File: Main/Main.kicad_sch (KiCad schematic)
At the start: 58 parts, among them J1 Conn_02x16_Odd_Even, J2 TYPE-C 6P, Q3 S9013 J3(RANGE:200-350), SW2 SS-12D11G3R, U1 BQ24074RGT, U2 DRV8833PW, U3 HUSB237-AA001-DN06R, U4 RT9742GGJ5, U5 RT9742GGJ5, U6 INA219AxDCN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

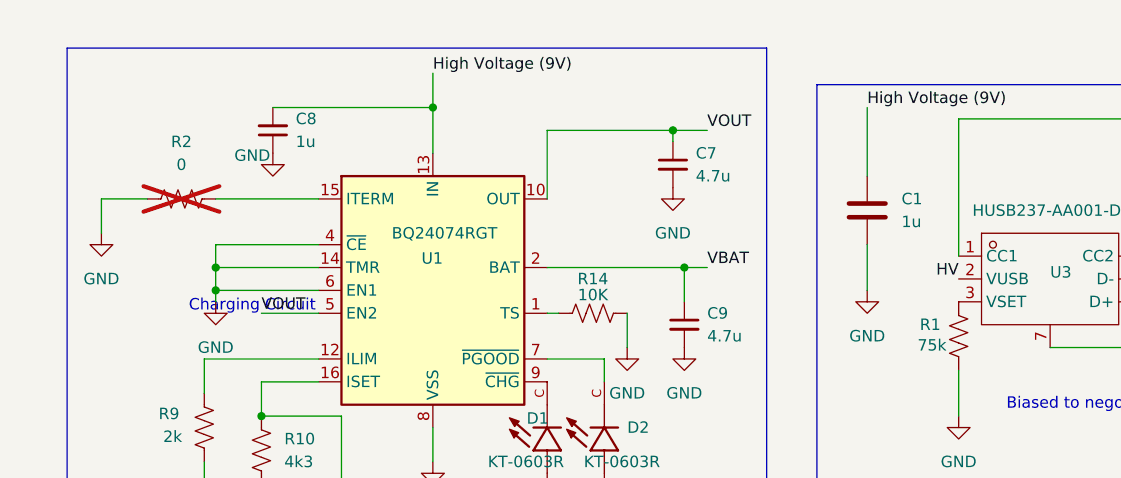
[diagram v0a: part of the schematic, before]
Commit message: Some few fixes on pin assignments
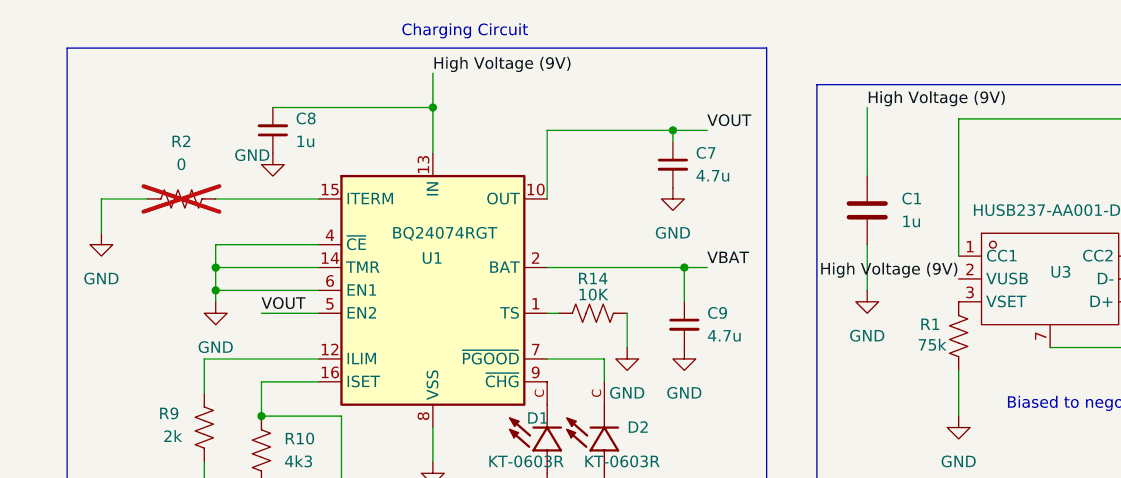
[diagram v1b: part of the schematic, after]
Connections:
- net HV is gone; now on net High Voltage (9V): U3.2 (VUSB)
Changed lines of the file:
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@@
 	(text "Charging Circuit\n"
 		(exclude_from_sim no)
-		(at 66.294 44.958 0)
+		(at 89.916 14.478 0)
 		(effects
 			(font
@@
 	(wire
 		(pts
+			(xy 140.97 218.44) (xy 140.97 220.98)
+		)
+		(stroke
+			(width 0)
+			(type default)
+		)
+	)
+	(wire
+		(pts
+			(xy 163.83 93.98) (xy 162.56 93.98)
+		)
+		(stroke
+			(width 0)
+			(type default)
+		)
+	)
+	(wire
+		(pts
+			(xy 364.49 58.42) (xy 389.89 58.42)
+		)
+		(stroke
+			(width 0)
+			(type default)
+		)
+	)
+	(wire
+		(pts
+			(xy 196.85 172.72) (xy 200.66 172.72)
+		)
+		(stroke
+			(width 0)
+			(type default)
+		)
+	)
+	(wire
+		(pts
+			(xy 217.17 232.41) (xy 220.98 232.41)
+		)
+		(stroke
+			(width 0)
+			(type default)
+		)
+	)
+	(wire
+		(pts
+			(xy 162.56 99.06) (xy 162.56 93.98)
+		)
+		(stroke
+			(width 0)
+			(type default)
+		)
+	)
+	(wire
+		(pts
 			(xy 190.5 41.91) (xy 194.31 41.91)
-		)
-		(stroke
-			(width 0)
-			(type default)
-		)
-	)
-	(wire
-		(pts
-			(xy 140.97 218.44) (xy 140.97 220.98)
-		)
-		(stroke
-			(width 0)
-			(type default)
-		)
-	)
-	(wire
-		(pts
-			(xy 163.83 93.98) (xy 162.56 93.98)
-		)
-		(stroke
-			(width 0)
-			(type default)
-		)
-	)
-	(wire
-		(pts
-			(xy 364.49 58.42) (xy 389.89 58.42)
-		)
-		(stroke
-			(width 0)
-			(type default)
-		)
-	)
-	(wire
-		(pts
-			(xy 196.85 172.72) (xy 200.66 172.72)
-		)
-		(stroke
-			(width 0)
-			(type default)
-		)
-	)
-	(wire
-		(pts
-			(xy 217.17 232.41) (xy 220.98 232.41)
-		)
-		(stroke
-			(width 0)
-			(type default)
-		)
-	)
-	(wire
-		(pts
-			(xy 162.56 99.06) (xy 162.56 93.98)
 		)
 		(stroke
@@
 		)
 	)
-	(label "HV"
+	(label "High Voltage (9V)"
 		(at 144.78 41.91 180)
 		(effects

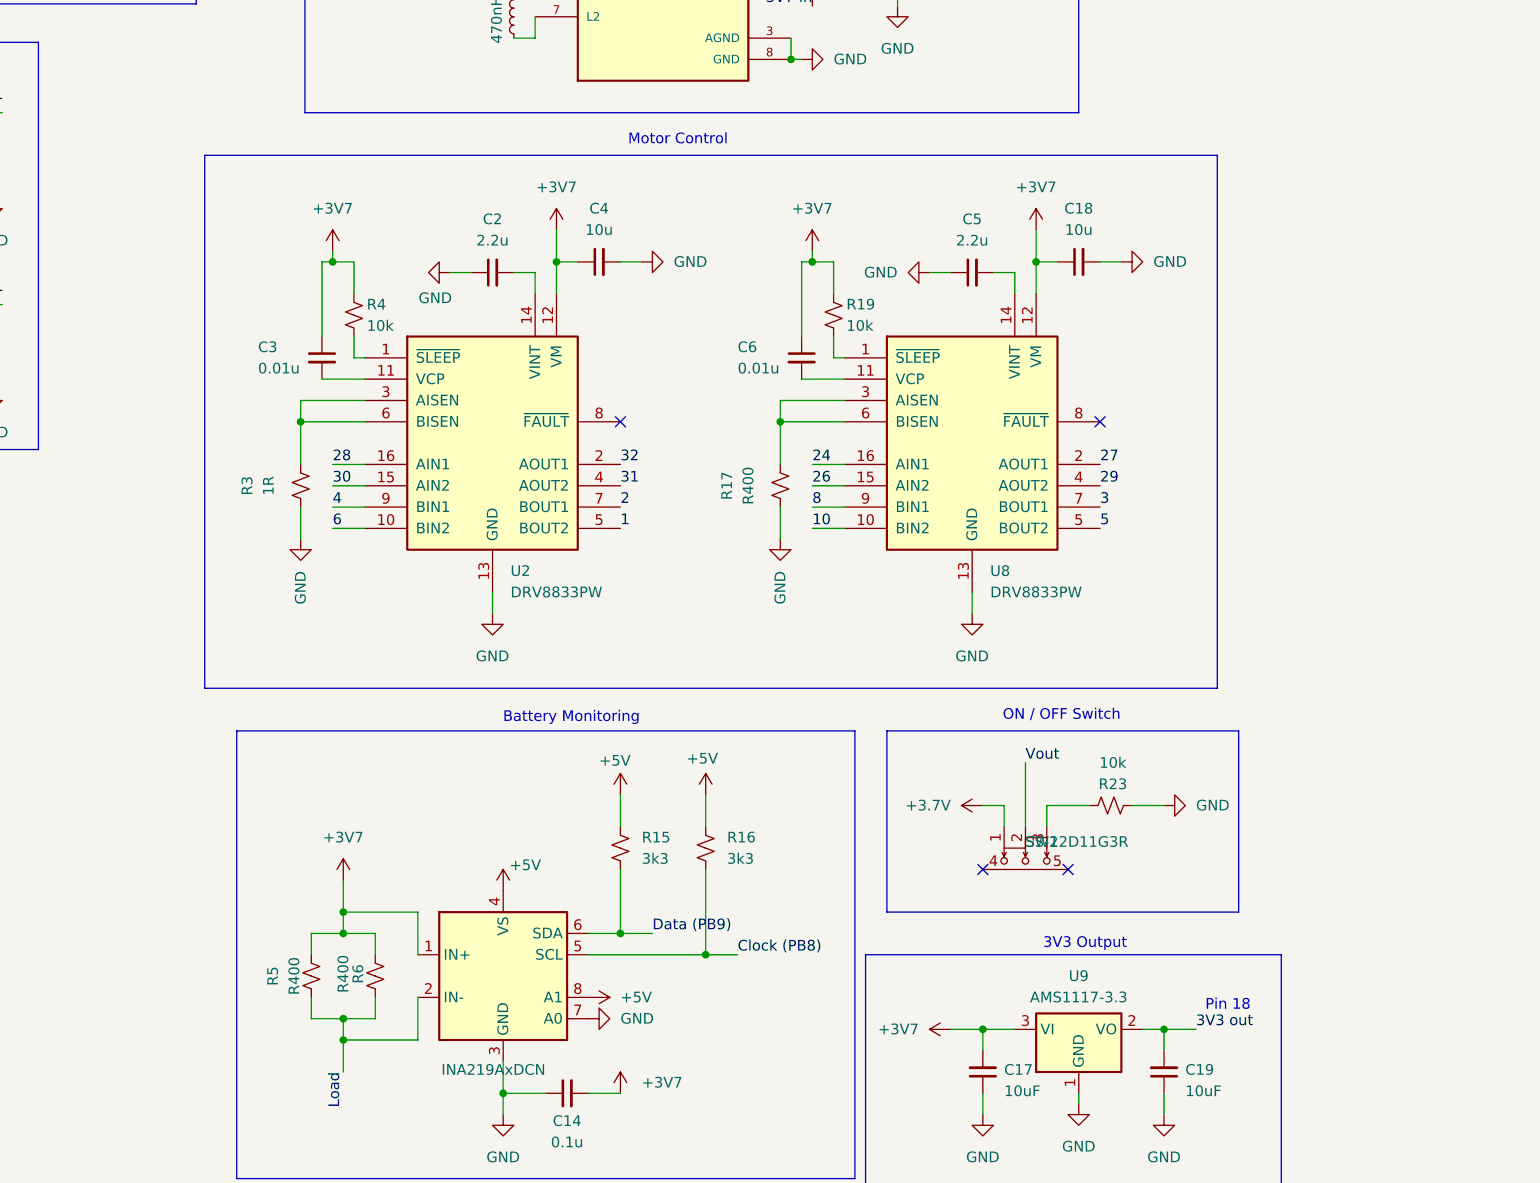
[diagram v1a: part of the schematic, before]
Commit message: Changed pins
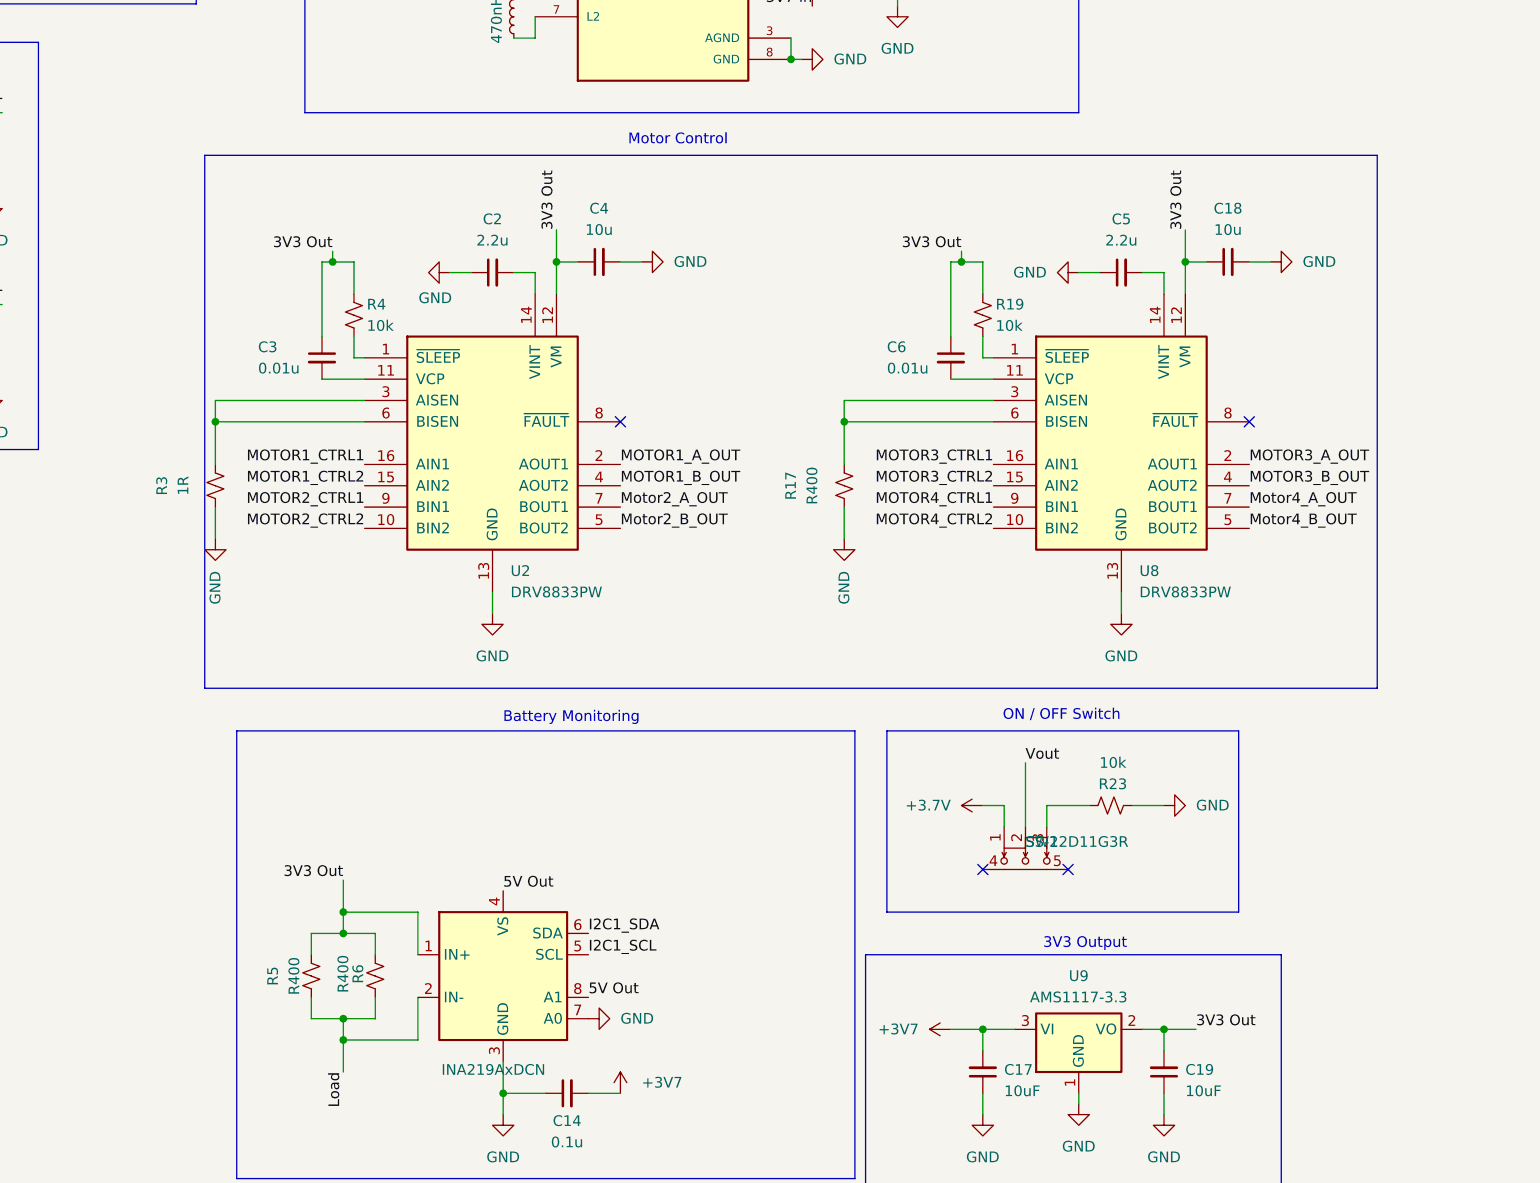
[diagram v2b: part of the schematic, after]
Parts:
- removed R15, R16: 3k3, Resistor_SMD:R_0603_1608Metric_Pad0.98x0.95mm_HandSolder, symbol Device:R_Small_US
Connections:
- net +5V is gone; now on net 5V Out: U6.4 (VS), U6.8 (A1)
- net 1 is gone; now on net Motor2_B_OUT: U2.5 (BOUT2)
- net 10 is gone; now on net MOTOR4_CTRL2: U8.10 (BIN2)
- net 2 is gone; now on net Motor2_A_OUT: U2.7 (BOUT1)
- net 24 is gone; now on net MOTOR3_CTRL1: U8.16 (AIN1)
- net 26 is gone; now on net MOTOR3_CTRL2: U8.15 (AIN2)
- net 27 is gone; now on net MOTOR3_A_OUT: U8.2 (AOUT1)
- net 28 is gone; now on net MOTOR1_CTRL1: U2.16 (AIN1)
- net 29 is gone; now on net MOTOR3_B_OUT: U8.4 (AOUT2)
- net 3 is gone; now on net Motor4_A_OUT: U8.7 (BOUT1)
- net 30 is gone; now on net MOTOR1_CTRL2: U2.15 (AIN2)
- net 31 is gone; now on net MOTOR1_B_OUT: U2.4 (AOUT2)
- net 32 is gone; now on net MOTOR1_A_OUT: U2.2 (AOUT1)
- net 3V3 out is gone; now on net 3V3 Out: C19.2, U9.2 (VO)
- net 4 is gone; now on net MOTOR2_CTRL1: U2.9 (BIN1)
- net 5 is gone; now on net Motor4_B_OUT: U8.5 (BOUT2)
- net 6 is gone; now on net MOTOR2_CTRL2: U2.10 (BIN2)
- net 8 is gone; now on net MOTOR4_CTRL1: U8.9 (BIN1)
- net Clock (PB8) is gone; now on net I2C1_SCL: U6.5 (SCL)
- net Data (PB9) is gone; now on net I2C1_SDA: U6.6 (SDA)
- net +3V7: no longer C18.1, C3.1, C4.1, C6.1, R19.1, R4.1, R5.2, R6.2, U2.12 (VM), U6.1 (IN+), U8.12 (VM)
- net 3V3 Out: now also C18.1, C3.1, C4.1, C6.1, R19.1, R4.1, R5.2, R6.2, U2.12 (VM), U6.1 (IN+), U8.12 (VM)
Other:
- note removed: "Pin 18"
- moved on the sheet: C18, C5, C6, R17, R19, R3, U8

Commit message: Changed Some Pin Names
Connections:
- net VBAT is gone; now on net Battery: C9.1, U1.2 (BAT), U1.3 (BAT)
- net Vout is gone; now on net switch: SW2.2
- net +3V7: no longer C17.2, U9.3 (VI)
- net 3V7 in renamed switch
- net switch: now also C17.2, U9.3 (VI)
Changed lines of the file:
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@@
 	(wire
 		(pts
+			(xy 196.85 110.49) (xy 196.85 113.03)
+		)
+		(stroke
+			(width 0)
+			(type default)
+		)
+	)
+	(wire
+		(pts
 			(xy 99.06 148.59) (xy 99.06 156.21)
 		)
@@
 		)
 	)
+	(label "switch"
+		(at 162.56 90.17 0)
+		(effects
+			(font
+				(size 1.27 1.27)
+			)
+			(justify left bottom)
+		)
+	)
 	(label "MOTOR2_CTRL2"
 		(at 351.79 35.56 180)
@@
 		)
 	)
-	(label "3V7 in"
-		(at 196.85 110.49 180)
+	(label "MOTOR3_B_OUT"
+		(at 248.92 167.64 0)
 		(effects
 			(font
 				(size 1.27 1.27)
 			)
-			(justify right bottom)
+			(justify left bottom)
 		)
 	)
-	(label "MOTOR3_B_OUT"
-		(at 248.92 167.64 0)
+	(label "switch"
+		(at 196.85 113.03 0)
 		(effects
 			(font
@@
 		)
 	)
-	(label "Vout"
+	(label "switch"
 		(at 222.25 200.66 0)
 		(effects
@@
 		)
 	)
-	(label "3V7 in"
-		(at 162.56 90.17 180)
-		(effects
-			(font
-				(size 1.27 1.27)
-			)
-			(justify right bottom)
-		)
-	)
-	(label "VBAT"
+	(label "Battery"
 		(at 116.84 40.64 0)
 		(effects
@@
 		)
 	)
+	(label "switch"
+		(at 213.36 232.41 180)
+		(effects
+			(font
+				(size 1.27 1.27)
+			)
+			(justify right bottom)
+		)
+	)
 	(symbol
 		(lib_id "Device:R_US")
@@
 					(unit 1)
 				)
-			)
-		)
-	)
-	(symbol
-		(lib_id "power:+3V8")
-		(at 213.36 232.41 90)
-		(unit 1)
-		(exclude_from_sim no)
-		(in_bom yes)
-		(on_board yes)
-		(dnp no)
-		(fields_autoplaced yes)
-		(property "Reference" "#PWR043"
-			(at 217.17 232.41 0)
-			(effects
-				(font
-					(size 1.27 1.27)
-				)
-				(hide yes)
-			)
-		)
-		(property "Value" "+3V7"
-			(at 209.55 232.4099 90)
-			(effects
-				(font
-					(size 1.27 1.27)
-				)
-				(justify left)
-			)
-		)
-		(property "Footprint" ""
-			(at 213.36 232.41 0)
-			(effects
-				(font
-					(size 1.27 1.27)
-				)
-				(hide yes)
-			)
-		)
-		(property "Datasheet" ""
-			(at 213.36 232.41 0)
-			(effects
-				(font
-					(size 1.27 1.27)
-				)
-				(hide yes)
-			)
-		)
-		(property "Description" "Power symbol creates a global label with name \"+3V8\""
-			(at 213.36 232.41 0)
-			(effects
-				(font
-					(size 1.27 1.27)
-				)
-				(hide yes)
-			)
-		)
-		(pin "1"
-		)
-		(instances
-			(project "Main"
-				(path "/0f55449c-8e79-4f10-a328-a1bcb934c334"
-					(reference "#PWR043")
-					(unit 1)
-				)

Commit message: Made some pin label changes
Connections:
- net +3.7V is gone; now on net Battery: SW2.1
- net +3V7 is gone; now on net Battery: C14.2
- net 5V out is gone; now on net 5V Out: C15.1, C16.1, R22.2, U7.6 (VOUT)
- no-connect marks 9 -> 11
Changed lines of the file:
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@@
 	)
 	(junction
-		(at 193.04 44.45)
-		(diameter 0)
-		(color 0 0 0 0)
-	)
-	(junction
 		(at 241.3 140.97)
 		(diameter 0)
@@
 	)
 	(no_connect
+		(at 351.79 43.18)
+	)
+	(no_connect
 		(at 364.49 48.26)
 	)
@@
 	)
 	(no_connect
+		(at 364.49 40.64)
+	)
+	(no_connect
 		(at 83.82 151.13)
 	)
@@
 	(wire
 		(pts
+			(xy 194.31 44.45) (xy 194.31 53.34)
+		)
+		(stroke
+			(width 0)
+			(type default)
+		)
+	)
+	(wire
+		(pts
 			(xy 207.01 99.06) (xy 194.31 99.06)
 		)
@@
 	(wire
 		(pts
-			(xy 193.04 31.75) (xy 193.04 44.45)
-		)
-		(stroke
-			(width 0)
-			(type default)
-		)
-	)
-	(wire
-		(pts
 			(xy 163.83 144.78) (xy 163.83 142.24)
 		)
@@
 	(wire
 		(pts
-			(xy 193.04 44.45) (xy 194.31 44.45)
-		)
-		(stroke
-			(width 0)
-			(type default)
-		)
-	)
-	(wire
-		(pts
 			(xy 100.33 146.05) (xy 83.82 146.05)
 		)
@@
 	(wire
 		(pts
-			(xy 193.04 44.45) (xy 193.04 49.53)
+			(xy 193.04 31.75) (xy 193.04 49.53)
 		)
 		(stroke
@@
 		)
 	)
-	(label "Motor2_A_OUT"
-		(at 173.99 170.18 0)
+	(label "5V Out"
+		(at 219.71 90.17 0)
 		(effects
 			(font
@@
 		)
 	)
-	(label "High Voltage (9V)"
-		(at 86.36 19.05 0)
+	(label "Motor2_A_OUT"
+		(at 173.99 170.18 0)
 		(effects
 			(font
@@
 		)
 	)
-	(label "5V out"
-		(at 219.71 90.17 0)
+	(label "High Voltage (9V)"
+		(at 86.36 19.05 0)
 		(effects
 			(font
@@
 		)
 	)
-	(label "5V out"
-		(at 194.31 93.98 0)
-		(effects
-			(font
-				(size 1.27 1.27)
-			)
-			(justify left bottom)
-		)
-	)
 	(label "Motor4_A_OUT"
 		(at 248.92 170.18 0)
@@
 		)
 	)
+	(label "5V Out"
+		(at 194.31 93.98 0)
+		(effects
+			(font
+				(size 1.27 1.27)
+			)
+			(justify left bottom)
+		)
+	)
 	(label "MOTOR3_CTRL1"
 		(at 218.44 165.1 180)
@@
 		)
 	)
+	(label "Battery"
+		(at 173.99 240.03 0)
+		(effects
+			(font
+				(size 1.27 1.27)
+			)
+			(justify left bottom)
+		)
+	)
 	(label "MOTOR2_CTRL1"
 		(at 351.79 33.02 180)
@@
 		)
 	)
+	(label "Battery"
+		(at 217.17 205.74 180)
+		(effects
+			(font
+				(size 1.27 1.27)
+			)
+			(justify right bottom)
+		)
+	)
 	(label "switch"
 		(at 213.36 232.41 180)
@@
 	)
 	(symbol
-		(lib_id "power:+3V8")
-		(at 173.99 240.03 0)
-		(unit 1)
-		(exclude_from_sim no)
-		(in_bom yes)
-		(on_board yes)
-		(dnp no)
-		(fields_autoplaced yes)
-		(property "Reference" "#PWR033"
-			(at 173.99 243.84 0)
-			(effects
-				(font
-					(size 1.27 1.27)
-				)
-				(hide yes)
-			)
-		)
-		(property "Value" "+3V7"
-			(at 176.53 238.7599 0)
-			(effects
-				(font
-					(size 1.27 1.27)
-				)
-				(justify left)
-			)
-		)
-		(property "Footprint" ""
-			(at 173.99 240.03 0)
-			(effects
-				(font
-					(size 1.27 1.27)
-				)
-				(hide yes)
-			)
-		)
-		(property "Datasheet" ""
-			(at 173.99 240.03 0)
-			(effects
-				(font
-					(size 1.27 1.27)
-				)
-				(hide yes)
-			)
-		)
-		(property "Description" "Power symbol creates a global label with name \"+3V8\""
-			(at 173.99 240.03 0)
-			(effects
-				(font
-					(size 1.27 1.27)
-				)
-				(hide yes)
-			)
-		)
-		(pin "1"
-		)
-		(instances
-			(project "Main"
-				(path "/0f55449c-8e79-4f10-a328-a1bcb934c334"
-					(reference "#PWR033")
-					(unit 1)
-				)
-			)
-		)
-	)
-	(symbol
 		(lib_id "Device:R_Small_US")
 		(at 217.17 147.32 0)
@@
 	)
 	(symbol
-		(lib_id "power:+3.3V")
-		(at 217.17 205.74 90)
-		(unit 1)
-		(exclude_from_sim no)
-		(in_bom yes)
-		(on_board yes)
-		(dnp no)
-		(fields_autoplaced yes)
-		(property "Reference" "#PWR045"
-			(at 220.98 205.74 0)
-			(effects
-				(font
-					(size 1.27 1.27)
-				)
-				(hide yes)
-			)
-		)
-		(property "Value" "+3.7V"
-			(at 213.36 205.7399 90)
-			(effects
-				(font
-					(size 1.27 1.27)
-				)
-				(justify left)
-			)
-		)
-		(property "Footprint" ""
-			(at 217.17 205.74 0)
-			(effects
-				(font
-					(size 1.27 1.27)
-				)
-				(hide yes)
-			)
-		)
-		(property "Datasheet" ""
-			(at 217.17 205.74 0)
-			(effects
-				(font
-					(size 1.27 1.27)
-				)
-				(hide yes)
-			)
-		)
-		(property "Description" "Power symbol creates a global label with name \"+3.3V\""
-			(at 217.17 205.74 0)
-			(effects
-				(font
-					(size 1.27 1.27)
-				)
-				(hide yes)
-			)
-		)
-		(pin "1"
-		)
-		(instances
-			(project "Main"
-				(path "/0f55449c-8e79-4f10-a328-a1bcb934c334"
-					(reference "#PWR045")
-					(unit 1)
-				)
-			)
-		)
-	)
-	(symbol
 		(lib_id "power:GND")
 		(at 200.66 173.99 0)
@@
 					(unit 1)
 				)
+			)
+		)
+	)
+	(symbol
+		(lib_id "power:GND")
+		(at 194.31 53.34 0)
+		(unit 1)
+		(exclude_from_sim no)
+		(in_bom yes)
+		(on_board yes)
+		(dnp no)
+		(fields_autoplaced yes)
+		(property "Reference" "#PWR011"
+			(at 194.31 59.69 0)
+			(effects
+				(font
+					(size 1.27 1.27)
+				)
+				(hide yes)
+			)
+		)
+		(property "Value" "GND"
+			(at 194.31 58.42 0)
+			(effects
+				(font
+					(size 1.27 1.27)
+				)
+			)
+		)
+		(property "Footprint" ""
+			(at 194.31 53.34 0)
+			(effects
+				(font
+					(size 1.27 1.27)
+				)
+				(hide yes)
+			)
+		)
+		(property "Datasheet" ""
+			(at 194.31 53.34 0)
+			(effects
+				(font
+					(size 1.27 1.27)
+				)
+				(hide yes)
+			)
+		)
+		(property "Description" "Power symbol creates a global label with name \"GND\" , ground"
+			(at 194.31 53.34 0)
+			(effects
+				(font
+					(size 1.27 1.27)
+				)
+				(hide yes)
+			)
+		)
+		(pin "1"
+		)
+		(instances
+			(project ""
+				(path "/0f55449c-8e79-4f10-a328-a1bcb934c334"
+					(reference "#PWR011")
+					(unit 1)
+				)
